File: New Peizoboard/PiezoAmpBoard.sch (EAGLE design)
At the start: 89 parts, among them IC3 TL072D, IC5 TL072D, IC6 TL072D, IC7 TL072D, U1 ARDUINOR3-BPLACE, U2 MIC5219 3.3V, X1 22-23-2021, X2 22-23-2021

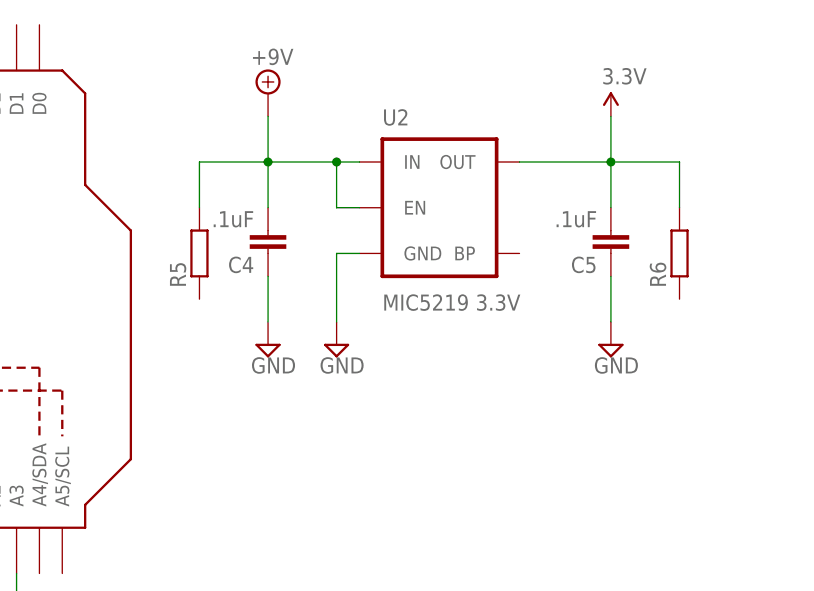
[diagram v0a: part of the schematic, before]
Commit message: add 9v and 3v indicator LEDs
From mac
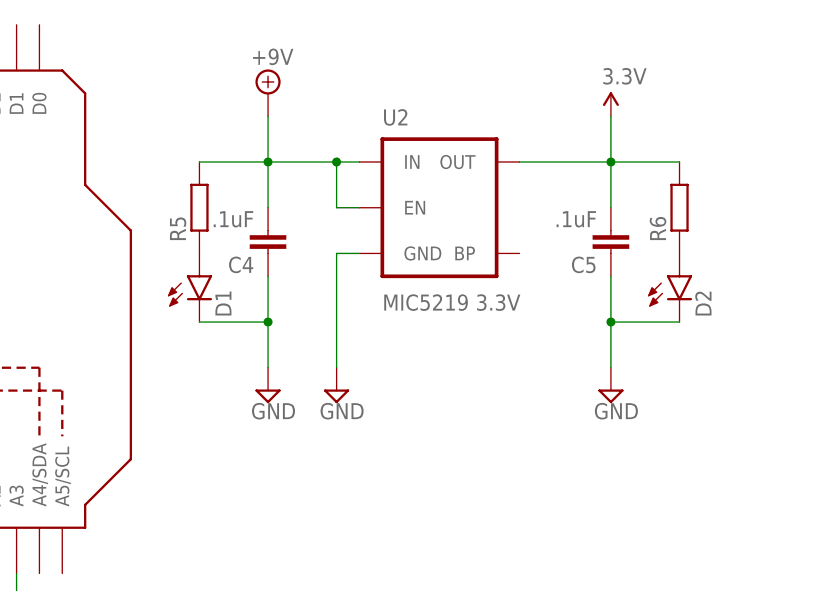
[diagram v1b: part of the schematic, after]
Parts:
- added D1, D2: (no value), SparkFun-LED:LED0603
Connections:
- new net N$1: D1.A, R5.1
- new net N$2: D2.A, R6.1
- net GND: now also D1.C, D2.C
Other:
- moved on the sheet: R5, R6
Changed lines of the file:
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@@
 <part name="R5" library="rcl" deviceset="R-EU_" device="R0603"/>
 <part name="R6" library="rcl" deviceset="R-EU_" device="R0603"/>
+<part name="D1" library="SparkFun-LED" deviceset="LED" device="0603"/>
+<part name="D2" library="SparkFun-LED" deviceset="LED" device="0603"/>
 </parts>
 <sheets>
@@
 <instance part="C5" gate="G$1" x="330.2" y="81.28" rot="R180"/>
 <instance part="SUPPLY83" gate="G$1" x="330.2" y="96.52"/>
-<instance part="SUPPLY84" gate="GND" x="292.1" y="71.12"/>
-<instance part="SUPPLY85" gate="GND" x="299.72" y="71.12"/>
-<instance part="SUPPLY86" gate="GND" x="330.2" y="71.12"/>
+<instance part="SUPPLY84" gate="GND" x="292.1" y="66.04"/>
+<instance part="SUPPLY85" gate="GND" x="299.72" y="66.04"/>
+<instance part="SUPPLY86" gate="GND" x="330.2" y="66.04"/>
 <instance part="SUPPLY87" gate="GND" x="208.28" y="154.94"/>
-<instance part="R5" gate="G$1" x="284.48" y="81.28" rot="R90"/>
-<instance part="R6" gate="G$1" x="337.82" y="81.28" rot="R90"/>
+<instance part="R5" gate="G$1" x="284.48" y="86.36" rot="R90"/>
+<instance part="R6" gate="G$1" x="337.82" y="86.36" rot="R90"/>
+<instance part="D1" gate="G$1" x="284.48" y="78.74"/>
+<instance part="D2" gate="G$1" x="337.82" y="78.74"/>
 </instances>
 <busses>
@@
 <junction x="330.2" y="91.44"/>
 <wire x1="330.2" y1="91.44" x2="337.82" y2="91.44" width="0.1524" layer="91"/>
-<wire x1="337.82" y1="91.44" x2="337.82" y2="86.36" width="0.1524" layer="91"/>
 <pinref part="R6" gate="G$1" pin="2"/>
 </segment>
@@
 <wire x1="292.1" y1="78.74" x2="292.1" y2="73.66" width="0.1524" layer="91"/>
 <pinref part="SUPPLY84" gate="GND" pin="GND"/>
+<pinref part="D1" gate="G$1" pin="C"/>
+<wire x1="292.1" y1="73.66" x2="292.1" y2="68.58" width="0.1524" layer="91"/>
+<wire x1="284.48" y1="73.66" x2="292.1" y2="73.66" width="0.1524" layer="91"/>
+<junction x="292.1" y="73.66"/>
 </segment>
 <segment>
 <pinref part="U2" gate="G$1" pin="GND"/>
 <wire x1="302.26" y1="81.28" x2="299.72" y2="81.28" width="0.1524" layer="91"/>
-<wire x1="299.72" y1="81.28" x2="299.72" y2="73.66" width="0.1524" layer="91"/>
+<wire x1="299.72" y1="81.28" x2="299.72" y2="68.58" width="0.1524" layer="91"/>
 <pinref part="SUPPLY85" gate="GND" pin="GND"/>
 </segment>
@@
 <wire x1="330.2" y1="78.74" x2="330.2" y2="73.66" width="0.1524" layer="91"/>
 <pinref part="SUPPLY86" gate="GND" pin="GND"/>
+<pinref part="D2" gate="G$1" pin="C"/>
+<wire x1="330.2" y1="73.66" x2="330.2" y2="68.58" width="0.1524" layer="91"/>
+<wire x1="337.82" y1="73.66" x2="330.2" y2="73.66" width="0.1524" layer="91"/>
+<junction x="330.2" y="73.66"/>
 </segment>
 <segment>
@@
 <junction x="299.72" y="91.44"/>
 <wire x1="292.1" y1="91.44" x2="284.48" y2="91.44" width="0.1524" layer="91"/>
-<wire x1="284.48" y1="91.44" x2="284.48" y2="86.36" width="0.1524" layer="91"/>
 <pinref part="R5" gate="G$1" pin="2"/>
 </segment>
 </net>
+<net name="N$1" class="0">
+<segment>
+<pinref part="R5" gate="G$1" pin="1"/>
+<pinref part="D1" gate="G$1" pin="A"/>
+</segment>
+</net>
+<net name="N$2" class="0">
+<segment>
+<pinref part="R6" gate="G$1" pin="1"/>
+<pinref part="D2" gate="G$1" pin="A"/>
+</segment>
+</net>

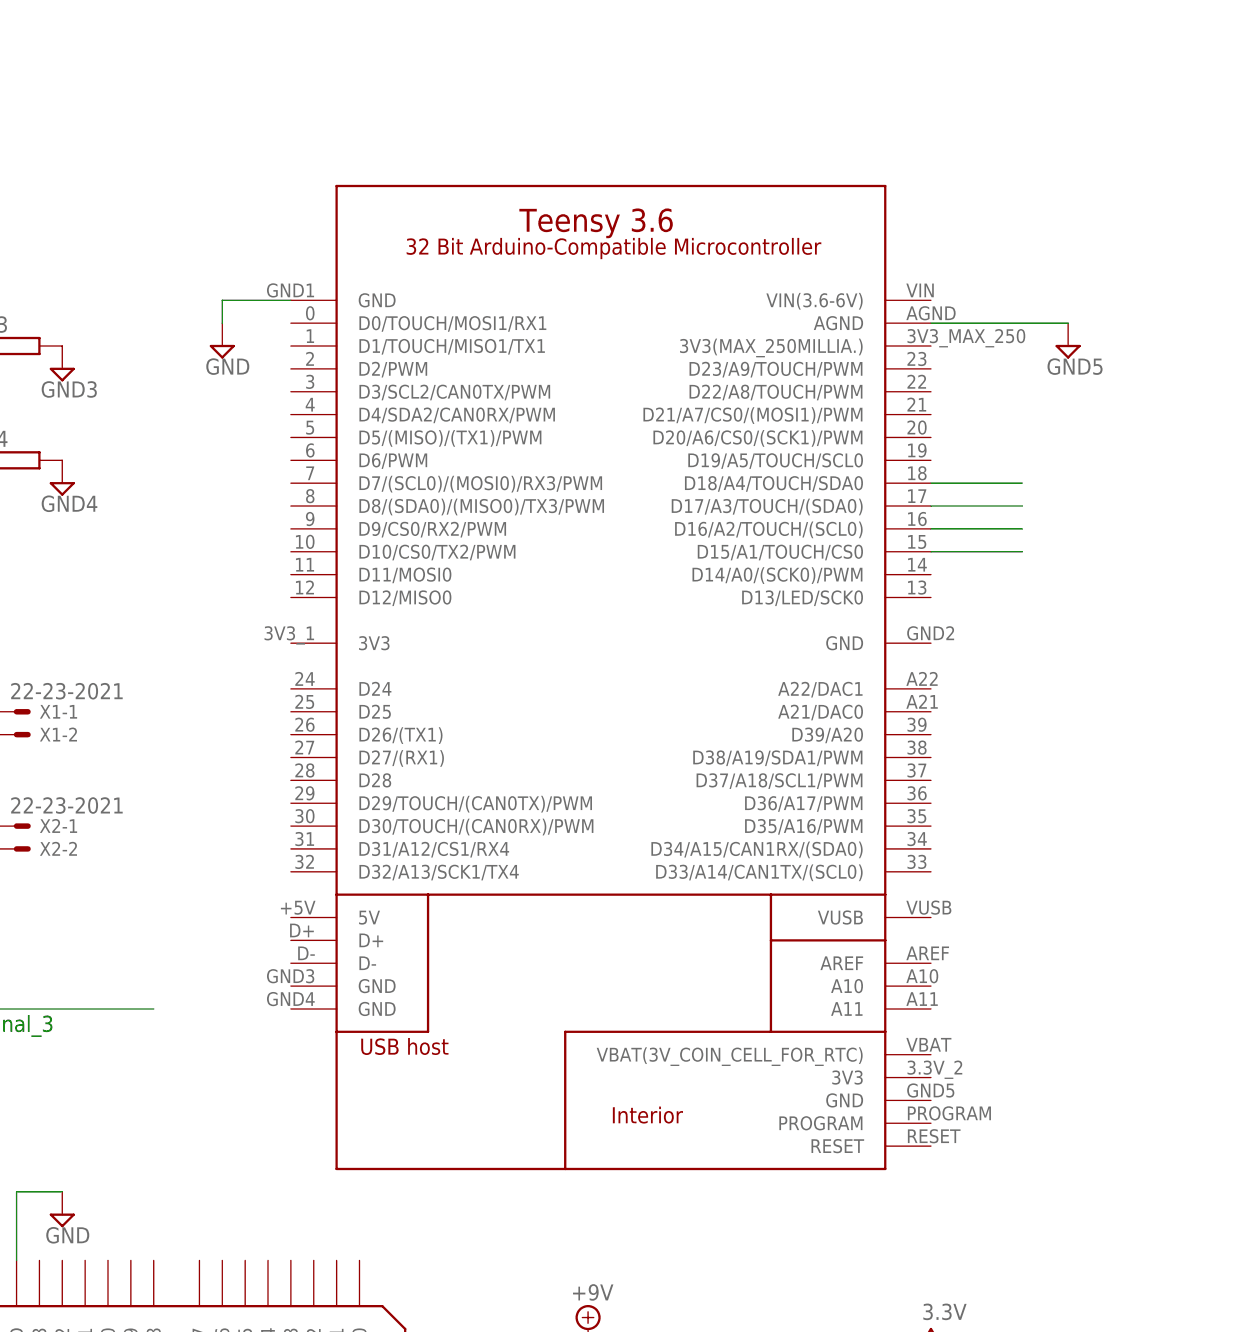
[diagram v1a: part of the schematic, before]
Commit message: add 3 teensy indicator LEDs
from pc
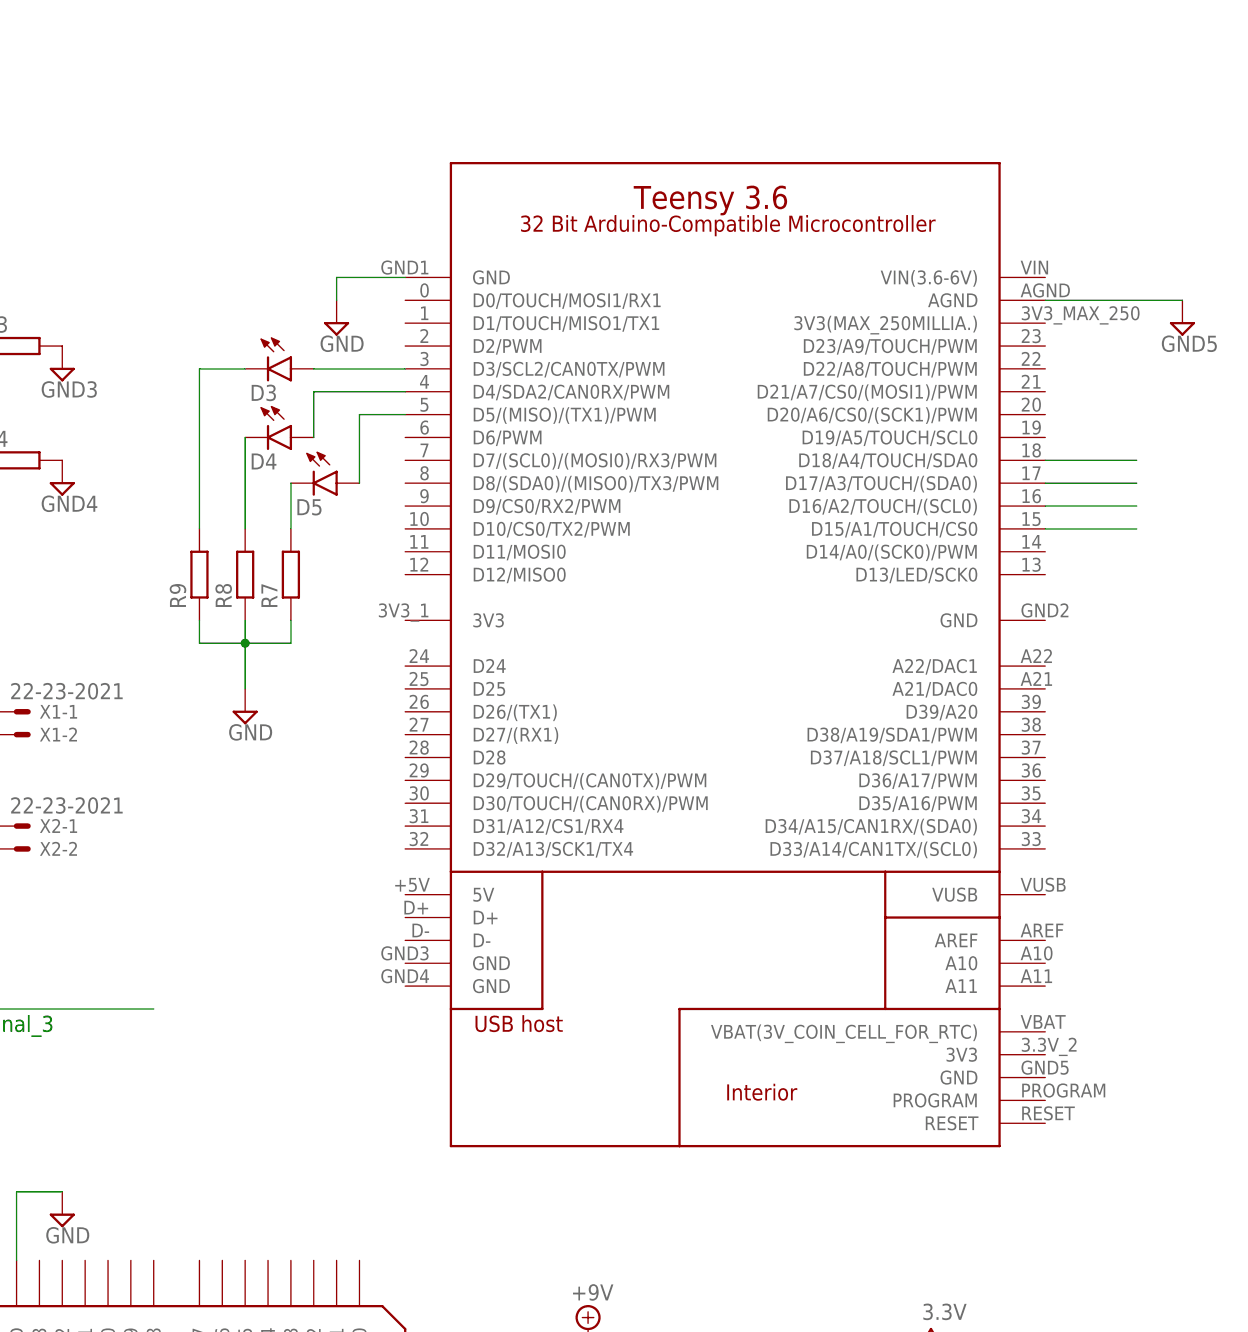
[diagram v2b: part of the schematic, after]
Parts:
- added D3, D4, D5: (no value), SparkFun-LED:LED0603
- added R7, R8, R9: (no value), rcl:R-EU_R0603
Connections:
- new net N$3: D3.A, U$2.D3/SCL2/CAN0TX/PWM
- new net N$4: D4.A, U$2.D4/SDA2/CAN0RX/PWM
- new net N$5: D5.A, U$2.D5/(MISO)/(TX1)/PWM
- new net N$6: D3.C, R9.2
- new net N$7: D4.C, R8.2
- new net N$8: D5.C, R7.2
- net GND: now also R7.1, R8.1, R9.1
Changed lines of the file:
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@@
 <?xml version="1.0" encoding="utf-8"?>
 <!DOCTYPE eagle SYSTEM "eagle.dtd">
-<eagle version="7.4.0">
+<eagle version="8.0.2">
 <drawing>
 <settings>
@@
 <part name="D1" library="SparkFun-LED" deviceset="LED" device="0603"/>
 <part name="D2" library="SparkFun-LED" deviceset="LED" device="0603"/>
+<part name="D3" library="SparkFun-LED" deviceset="LED" device="0603"/>
+<part name="D4" library="SparkFun-LED" deviceset="LED" device="0603"/>
+<part name="D5" library="SparkFun-LED" deviceset="LED" device="0603"/>
+<part name="R7" library="rcl" deviceset="R-EU_" device="R0603"/>
+<part name="R8" library="rcl" deviceset="R-EU_" device="R0603"/>
+<part name="R9" library="rcl" deviceset="R-EU_" device="R0603"/>
+<part name="SUPPLY70" library="supply2" deviceset="GND" device=""/>
 </parts>
 <sheets>
@@
 <instance part="R1" gate="G$1" x="213.36" y="195.58"/>
 <instance part="R2" gate="G$1" x="213.36" y="208.28"/>
-<instance part="U$2" gate="G$1" x="266.7" y="223.52"/>
-<instance part="SUPPLY80" gate="GND" x="251.46" y="208.28"/>
-<instance part="SUPPLY81" gate="G$1" x="345.44" y="208.28"/>
+<instance part="U$2" gate="G$1" x="279.4" y="226.06"/>
+<instance part="SUPPLY80" gate="GND" x="264.16" y="210.82"/>
+<instance part="SUPPLY81" gate="G$1" x="358.14" y="210.82"/>
 <instance part="U2" gate="G$1" x="312.42" y="86.36"/>
 <instance part="SUPPLY82" gate="G$1" x="292.1" y="99.06"/>
@@
 <instance part="D1" gate="G$1" x="284.48" y="78.74"/>
 <instance part="D2" gate="G$1" x="337.82" y="78.74"/>
+<instance part="D3" gate="G$1" x="259.08" y="205.74" rot="R270"/>
+<instance part="D4" gate="G$1" x="259.08" y="198.12" rot="R270"/>
+<instance part="D5" gate="G$1" x="264.16" y="193.04" rot="R270"/>
+<instance part="R7" gate="G$1" x="259.08" y="182.88" rot="R90"/>
+<instance part="R8" gate="G$1" x="254" y="182.88" rot="R90"/>
+<instance part="R9" gate="G$1" x="248.92" y="182.88" rot="R90"/>
+<instance part="SUPPLY70" gate="GND" x="254" y="167.64"/>
 </instances>
 <busses>
@@
 <segment>
 <pinref part="U$2" gate="G$1" pin="GND@1"/>
-<wire x1="259.08" y1="213.36" x2="251.46" y2="213.36" width="0.1524" layer="91"/>
-<wire x1="251.46" y1="213.36" x2="251.46" y2="210.82" width="0.1524" layer="91"/>
+<wire x1="271.78" y1="215.9" x2="264.16" y2="215.9" width="0.1524" layer="91"/>
+<wire x1="264.16" y1="215.9" x2="264.16" y2="213.36" width="0.1524" layer="91"/>
 <pinref part="SUPPLY80" gate="GND" pin="GND"/>
 </segment>
@@
 <pinref part="SUPPLY87" gate="GND" pin="GND"/>
 </segment>
+<segment>
+<pinref part="R9" gate="G$1" pin="1"/>
+<wire x1="248.92" y1="177.8" x2="248.92" y2="175.26" width="0.1524" layer="91"/>
+<wire x1="248.92" y1="175.26" x2="254" y2="175.26" width="0.1524" layer="91"/>
+<pinref part="R7" gate="G$1" pin="1"/>
+<wire x1="254" y1="175.26" x2="259.08" y2="175.26" width="0.1524" layer="91"/>
+<wire x1="259.08" y1="175.26" x2="259.08" y2="177.8" width="0.1524" layer="91"/>
+<pinref part="R8" gate="G$1" pin="1"/>
+<wire x1="254" y1="177.8" x2="254" y2="175.26" width="0.1524" layer="91"/>
+<wire x1="254" y1="175.26" x2="254" y2="170.18" width="0.1524" layer="91"/>
+<junction x="254" y="175.26"/>
+<pinref part="SUPPLY70" gate="GND" pin="GND"/>
+</segment>
 </net>
 <net name="VS+1" class="0">
@@
 <segment>
 <pinref part="U$2" gate="G$1" pin="D17/A3/TOUCH/(SDA0)"/>
-<wire x1="330.2" y1="190.5" x2="340.36" y2="190.5" width="0.1524" layer="91"/>
+<wire x1="342.9" y1="193.04" x2="353.06" y2="193.04" width="0.1524" layer="91"/>
 </segment>
 </net>
@@
 <segment>
 <pinref part="U$2" gate="G$1" pin="D15/A1/TOUCH/CS0"/>
-<wire x1="330.2" y1="185.42" x2="340.36" y2="185.42" width="0.1524" layer="91"/>
+<wire x1="342.9" y1="187.96" x2="353.06" y2="187.96" width="0.1524" layer="91"/>
 </segment>
 </net>
@@
 <segment>
 <pinref part="U$2" gate="G$1" pin="D16/A2/TOUCH/(SCL0)"/>
-<wire x1="330.2" y1="187.96" x2="340.36" y2="187.96" width="0.1524" layer="91"/>
+<wire x1="342.9" y1="190.5" x2="353.06" y2="190.5" width="0.1524" layer="91"/>
 </segment>
 </net>
@@
 <segment>
 <pinref part="U$2" gate="G$1" pin="D18/A4/TOUCH/SDA0"/>
-<wire x1="330.2" y1="193.04" x2="340.36" y2="193.04" width="0.1524" layer="91"/>
+<wire x1="342.9" y1="195.58" x2="353.06" y2="195.58" width="0.1524" layer="91"/>
 </segment>
 </net>
@@
 <pinref part="U$2" gate="G$1" pin="AGND"/>
 <pinref part="SUPPLY81" gate="G$1" pin="GND5"/>
-<wire x1="330.2" y1="210.82" x2="345.44" y2="210.82" width="0.1524" layer="91"/>
+<wire x1="342.9" y1="213.36" x2="358.14" y2="213.36" width="0.1524" layer="91"/>
 </segment>
 </net>
@@
 </segment>
 </net>
+<net name="N$3" class="0">
+<segment>
+<pinref part="U$2" gate="G$1" pin="D3/SCL2/CAN0TX/PWM"/>
+<pinref part="D3" gate="G$1" pin="A"/>
+<wire x1="271.78" y1="205.74" x2="261.62" y2="205.74" width="0.1524" layer="91"/>
+</segment>
+</net>
+<net name="N$4" class="0">
+<segment>
+<pinref part="U$2" gate="G$1" pin="D4/SDA2/CAN0RX/PWM"/>
+<wire x1="271.78" y1="203.2" x2="261.62" y2="203.2" width="0.1524" layer="91"/>
+<wire x1="261.62" y1="203.2" x2="261.62" y2="198.12" width="0.1524" layer="91"/>
+<pinref part="D4" gate="G$1" pin="A"/>
+</segment>
+</net>
+<net name="N$5" class="0">
+<segment>
+<pinref part="U$2" gate="G$1" pin="D5/(MISO)/(TX1)/PWM"/>
+<pinref part="D5" gate="G$1" pin="A"/>
+<wire x1="271.78" y1="200.66" x2="266.7" y2="200.66" width="0.1524" layer="91"/>
+<wire x1="266.7" y1="200.66" x2="266.7" y2="193.04" width="0.1524" layer="91"/>
+</segment>
+</net>
+<net name="N$6" class="0">
+<segment>
+<pinref part="D3" gate="G$1" pin="C"/>
+<pinref part="R9" gate="G$1" pin="2"/>
+<wire x1="254" y1="205.74" x2="248.92" y2="205.74" width="0.1524" layer="91"/>
+<wire x1="248.92" y1="205.74" x2="248.92" y2="187.96" width="0.1524" layer="91"/>
+</segment>
+</net>
+<net name="N$7" class="0">
+<segment>
+<pinref part="D4" gate="G$1" pin="C"/>
+<pinref part="R8" gate="G$1" pin="2"/>
+<wire x1="254" y1="198.12" x2="254" y2="187.96" width="0.1524" layer="91"/>
+</segment>
+</net>
+<net name="N$8" class="0">
+<segment>
+<pinref part="D5" gate="G$1" pin="C"/>
+<pinref part="R7" gate="G$1" pin="2"/>
+<wire x1="259.08" y1="193.04" x2="259.08" y2="187.96" width="0.1524" layer="91"/>
+</segment>
+</net>

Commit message: Add all parts, still need some wires, need serial connection
from pc
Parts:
- added J1: RJ45, SparkFun-Connectors:RJ45-8
- added U$3: MAX3491, BackplaneParts:MAX3491
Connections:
- new net N$10: J1.7, U$3.Z
- new net N$11: J1.6, U$3.B
- new net N$12: J1.5, U$3.A
- new net N$9: J1.8, U$3.Y
- net 3.3V: now also U$2.3V3(MAX_250MILLIA.), U$2.3V3@1, U$3.VCC13, U$3.VCC14
- net GND: now also U$3.GND6, U$3.GND7
- net N$3: now also U$2.D38/A19/SDA1/PWM; no longer U$2.D3/SCL2/CAN0TX/PWM
- net N$4: now also U$2.D37/A18/SCL1/PWM; no longer U$2.D4/SDA2/CAN0RX/PWM
- net N$5: now also U$2.D36/A17/PWM; no longer U$2.D5/(MISO)/(TX1)/PWM
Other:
- note added: "Signal_4"
- note removed: "Signal_0"
- moved on the sheet: D3, D4, D5, R7, R8, R9
